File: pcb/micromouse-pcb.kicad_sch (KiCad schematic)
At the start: 38 parts, among them Q1 BS170, Q2 TEFT4300, Q3 BS170, Q4 TEFT4300, Q5 BS170, Q6 TEFT4300, Q7 BS170, Q8 TEFT4300, SW1 SW_SPDT, U0 L7805, U1 Teensy 4.1

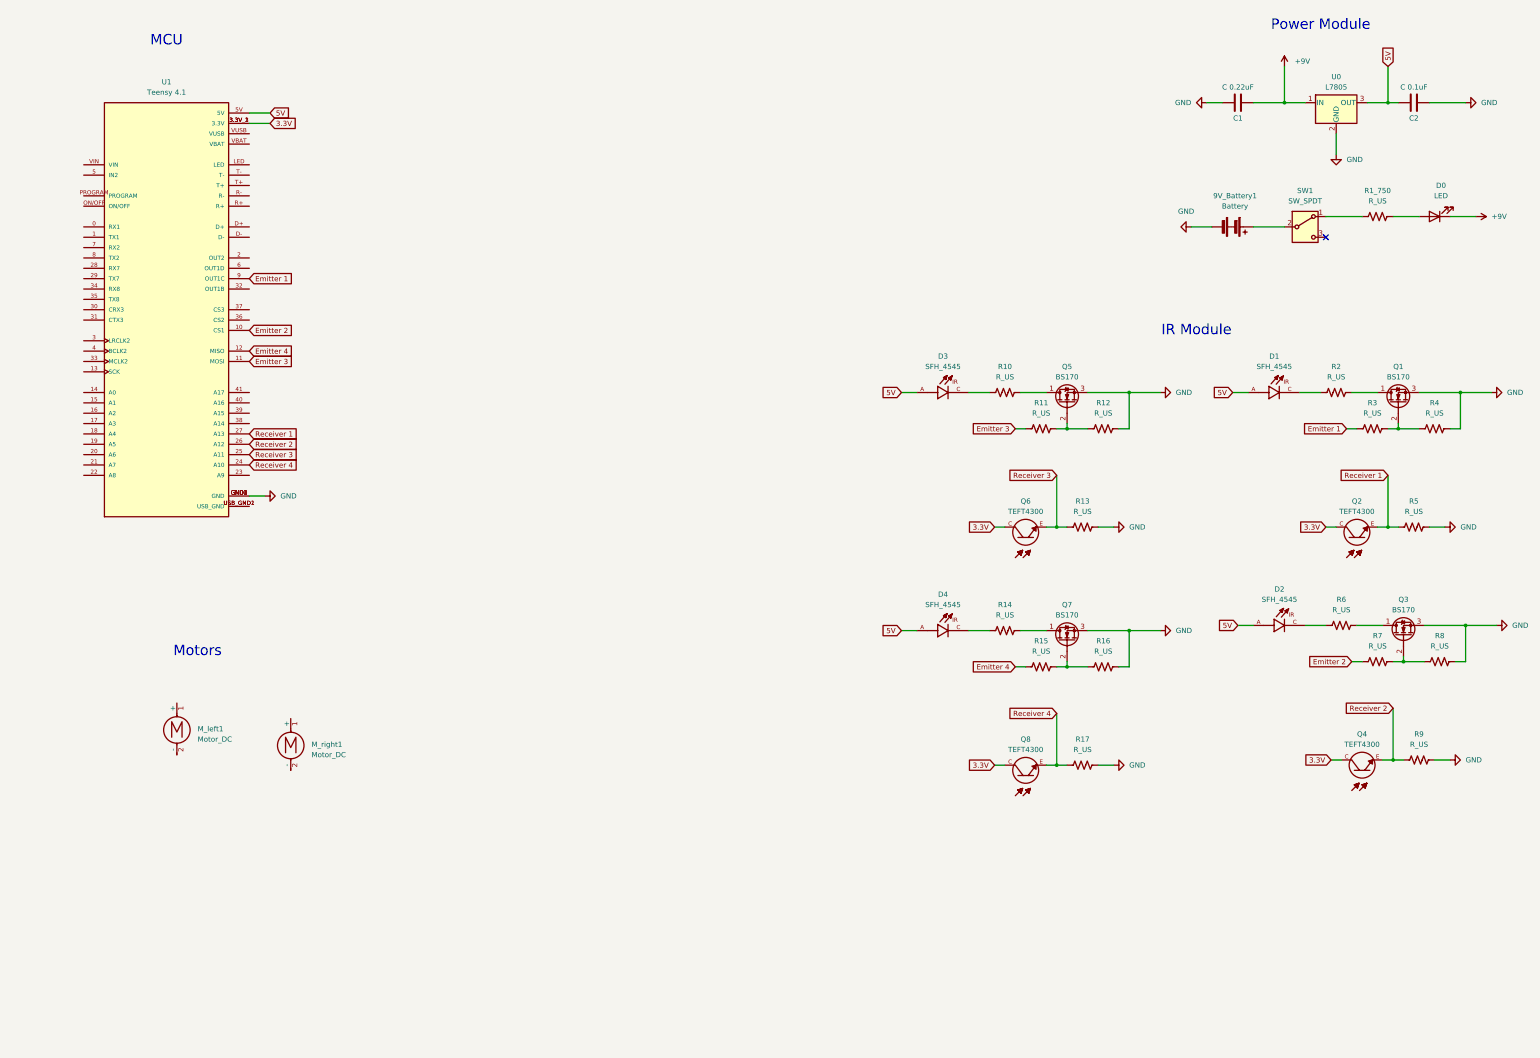
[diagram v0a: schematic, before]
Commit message: Fixing bad symbol library management
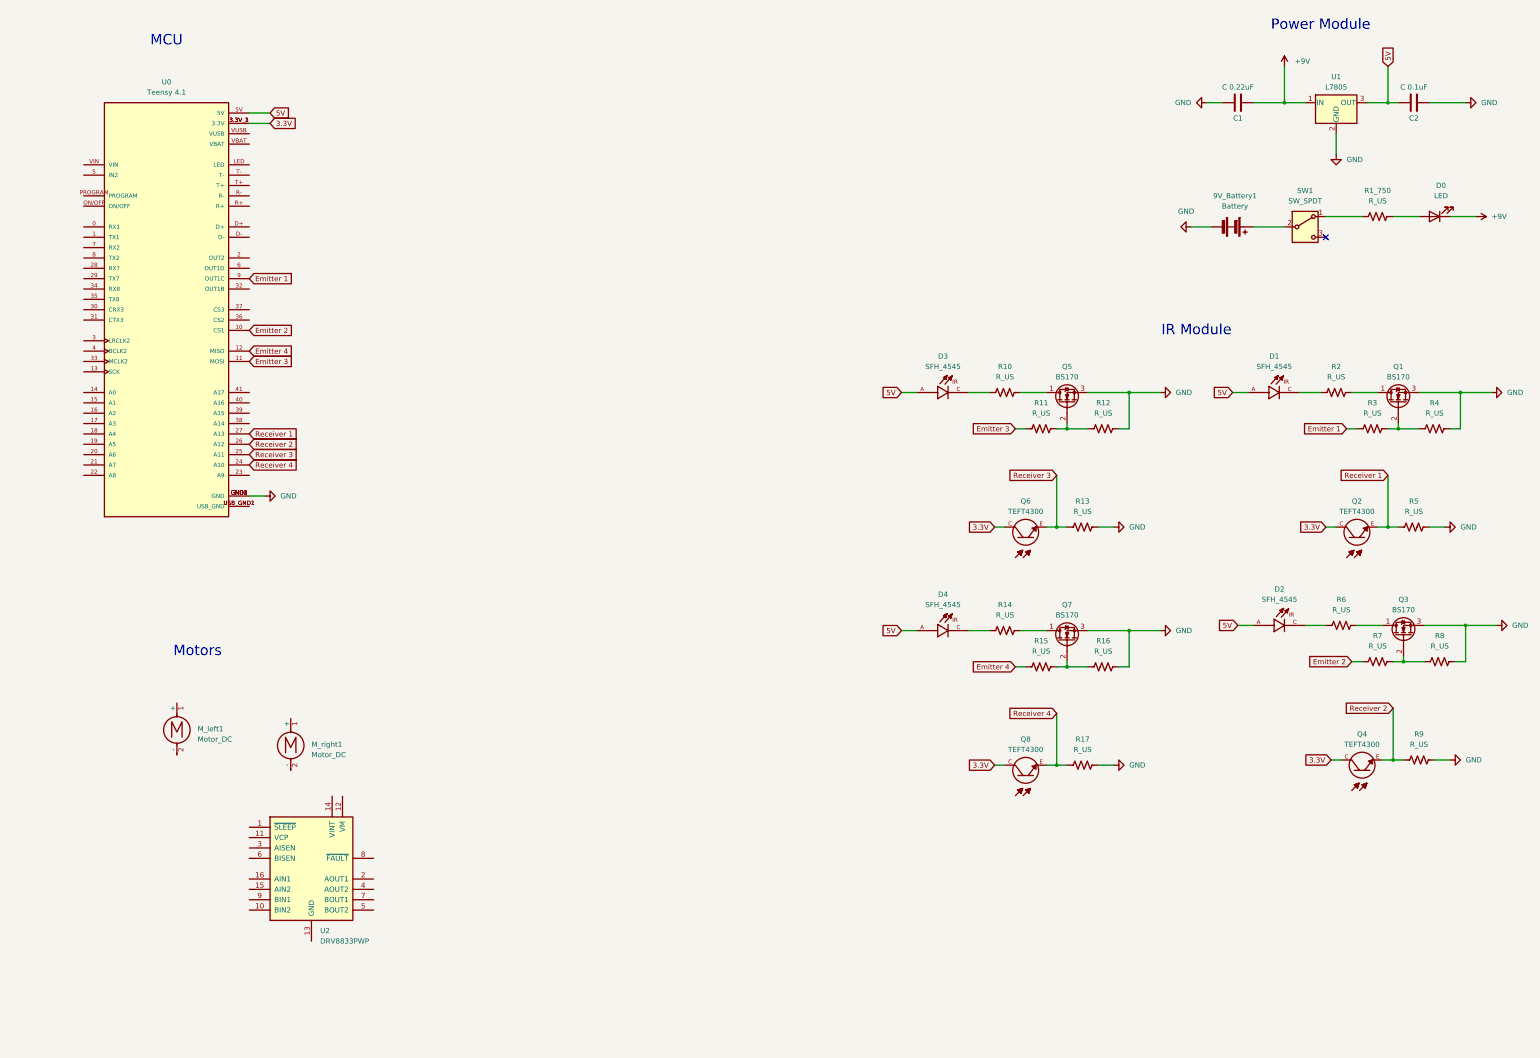
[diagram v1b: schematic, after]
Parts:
- added U2: DRV8833PWP, Package_SO:HTSSOP-16-1EP_4.4x5mm_P0.65mm_EP3.4x5mm_Mask2.46x2.31mm_ThermalVias, symbol Driver_Motor:DRV8833PWP
- renumbered U1 to U0, U0 to U1
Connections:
- new net: U2.13 (GND), U2.17 (GND)
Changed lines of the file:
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@@
 		(dnp no)
 		(fields_autoplaced yes)
-		(property "Reference" "U0"
+		(property "Reference" "U1"
 			(at 346.71 40.64 0)
 			(effects
@@
 			(project ""
 				(path "/6bab3514-b9e6-4652-bd2e-edc57bdbde3d"
-					(reference "U0")
+					(reference "U1")
 					(unit 1)
 				)
@@
 		(dnp no)
 		(fields_autoplaced yes)
-		(property "Reference" "U1"
+		(property "Reference" "U0"
 			(at 59.69 41.91 0)
 			(effects
@@
 			(project ""
 				(path "/6bab3514-b9e6-4652-bd2e-edc57bdbde3d"
-					(reference "U1")
+					(reference "U0")
 					(unit 1)
 				)
@@
 					(unit 1)
 				)
+			)
+		)
+	)
+	(symbol
+		(lib_id "Driver_Motor:DRV8833PWP")
+		(at 95.25 234.95 0)
+		(unit 1)
+		(exclude_from_sim no)
+		(in_bom yes)
+		(on_board yes)
+		(dnp no)
+		(fields_autoplaced yes)
+		(property "Reference" "U2"
+			(at 97.3933 250.19 0)
+			(effects
+				(font
+					(size 1.27 1.27)
+				)
+				(justify left)
+			)
+		)
+		(property "Value" "DRV8833PWP"
+			(at 97.3933 252.73 0)
+			(effects
+				(font
+					(size 1.27 1.27)
+				)
+				(justify left)
+			)
+		)
+		(property "Footprint" "Package_SO:HTSSOP-16-1EP_4.4x5mm_P0.65mm_EP3.4x5mm_Mask2.46x2.31mm_ThermalVias"
+			(at 100.33 250.19 0)
+			(effects
+				(font
+					(size 1.27 1.27)
+				)
+				(justify left)
+				(hide yes)
+			)
+		)
+		(property "Datasheet" "http://www.ti.com/lit/ds/symlink/drv8833.pdf"
+			(at 100.33 252.73 0)
+			(effects
+				(font
+					(size 1.27 1.27)
+				)
+				(justify left)
+				(hide yes)
+			)
+		)
+		(property "Description" "Dual H-Bridge Motor Driver, HTSSOP-16"
+			(at 95.25 234.95 0)
+			(effects
+				(font
+					(size 1.27 1.27)
+				)
+				(hide yes)
+			)
+		)
+		(pin "1"
+		)
+		(pin "11"
+		)
+		(pin "3"
+		)
+		(pin "6"
+		)
+		(pin "16"
+		)
+		(pin "15"
+		)
+		(pin "9"
+		)
+		(pin "10"
+		)
+		(pin "13"
+		)
+		(pin "17"
+		)
+		(pin "14"
+		)
+		(pin "12"
+		)
+		(pin "8"
+		)
+		(pin "2"
+		)
+		(pin "4"
+		)
+		(pin "7"
+		)
+		(pin "5"
+		)
+		(instances
+			(project ""
+				(path "/6bab3514-b9e6-4652-bd2e-edc57bdbde3d"
+					(reference "U2")
+					(unit 1)
+				)

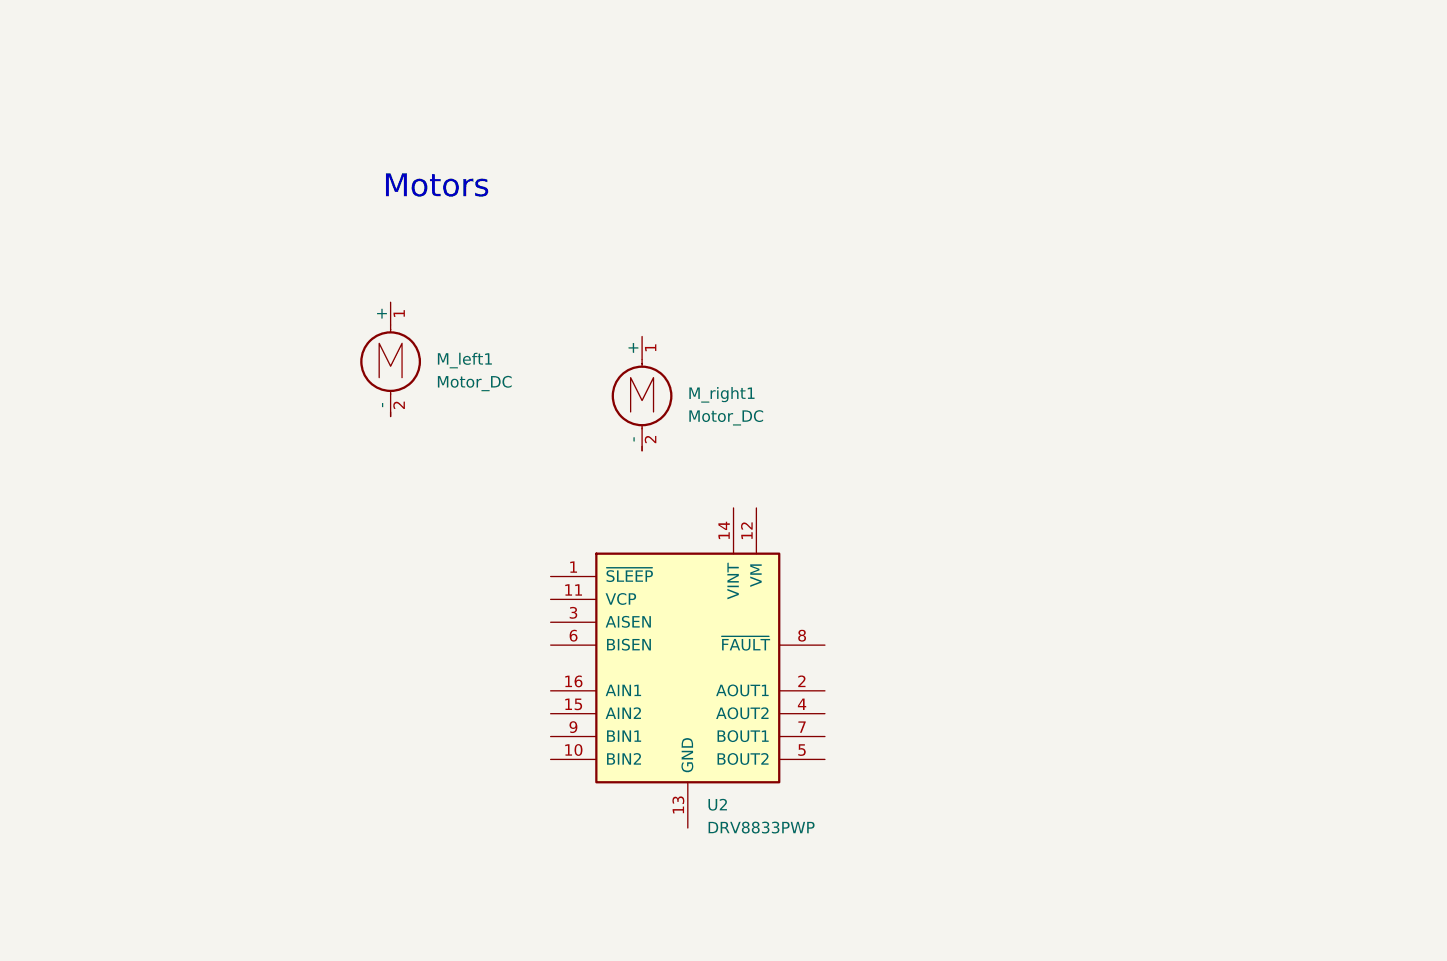
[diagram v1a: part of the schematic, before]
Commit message: motor module connectors
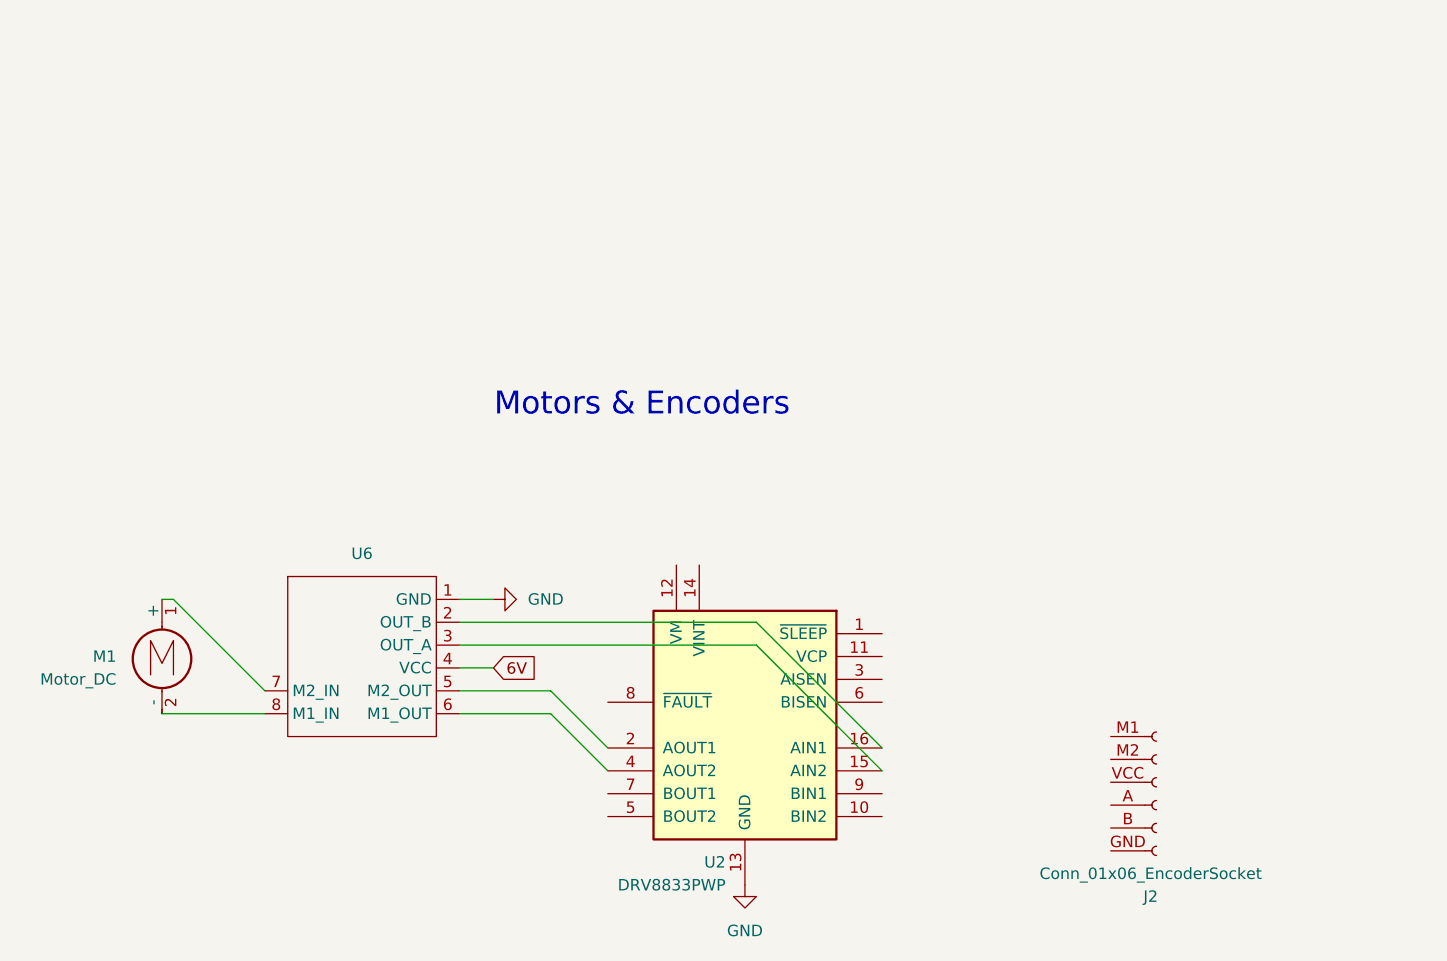
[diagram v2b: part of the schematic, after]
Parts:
- removed M_right1: Motor_DC, symbol Motor:Motor_DC
- added J2: Conn_01x06_EncoderSocket, symbol micromouse-symbols:Conn_01x06_EncoderSocket
- added U6: ~, symbol micromouse-symbols:Polulu_Encoder
- renumbered M_left1 to M1
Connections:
- net GND: now also U2.13 (GND), U2.17 (GND), U6.1 (GND)
- net at M1.1 (+): now also U6.7 (M2_IN)
- net at M1.2 (-): now also U6.8 (M1_IN)
- net at U2.15 (AIN2): now also U6.3 (OUT_A)
- net at U2.16 (AIN1): now also U6.2 (OUT_B)
- net at U2.2 (AOUT1): now also U6.5 (M2_OUT)
- net at U2.4 (AOUT2): now also U6.6 (M1_OUT)
- new net 6V: U6.4 (VCC)
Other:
- note added: "Motors & Encoders"
- note removed: "Motors"
- moved on the sheet: M1, U2
